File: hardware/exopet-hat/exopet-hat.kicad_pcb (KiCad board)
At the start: 2 copper layers, 65 x 56 mm, 71 parts, among them J1 BarrelJack_CUI_PJ-102AH_Horiz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, J10 TerminalBlock_Phoenix_PT-1,5-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, J11 TerminalBlock_Phoenix_PT-1,5-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, J13 TerminalBlock_Phoenix_PT-1,5-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, J14 TerminalBlock_Phoenix_PT-1,5-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, J3 PinSocket_2x20_P2.54mm_Vertic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, J4 TerminalBlock_Phoenix_PT-1,5-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, J8 TerminalBlock_Phoenix_PT-1,5-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, J9 TerminalBlock_Phoenix_PT-1,5-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, K1 Relay_SPDT_Omron-G5LE-1, K2 Relay_SPDT_Omron-G5LE-1, K3 Relay_SPDT_Omron-G5LE-1, K4 Relay_SPDT_Omron-G5LE-1, Q1 TO-252-2, U2 SOIC-16_3.9x9.9mm_P1.27mm, U4 SOIC-8_3.9x4.9mm_P1.27mm, U5 D_SOD-323, U6 SOT-23-6

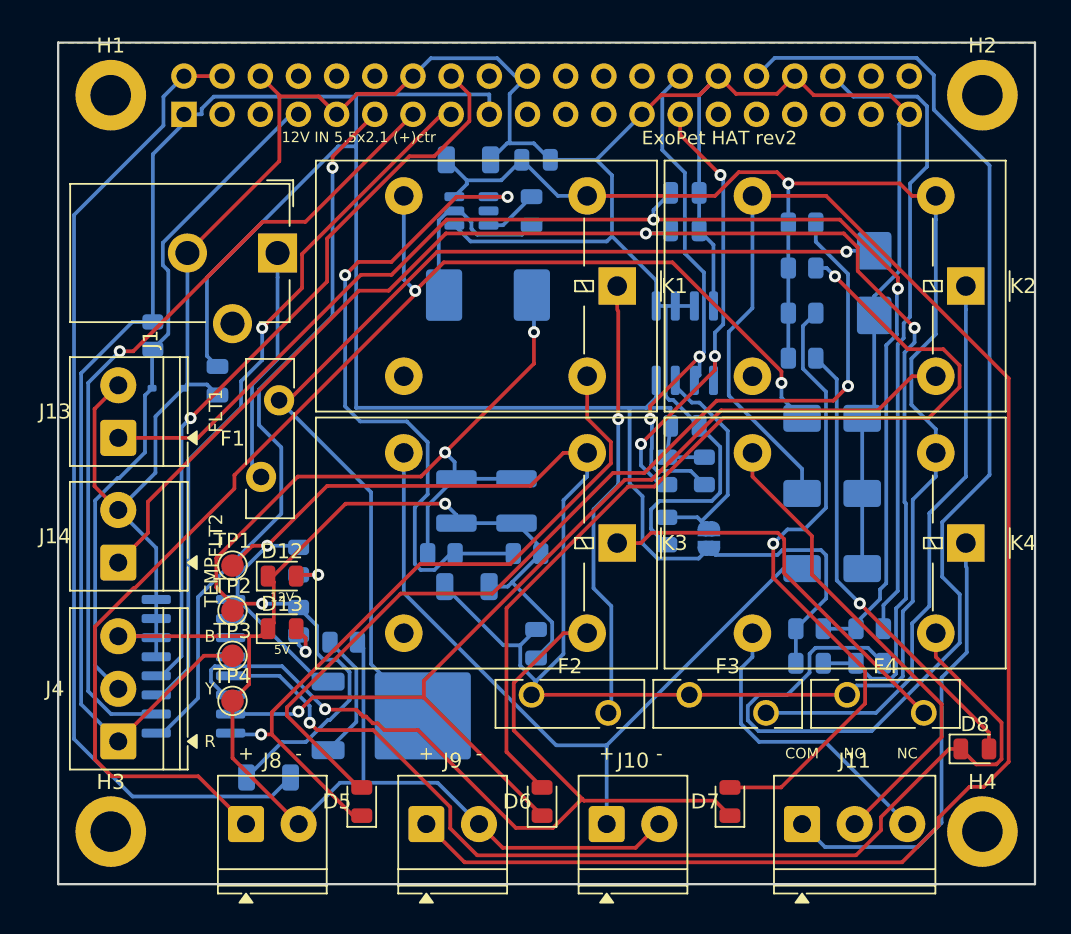
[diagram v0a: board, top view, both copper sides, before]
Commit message: HAT rev 2: apply all 7 fresh-eyes review fixes
- D3 B550C safety diode replaces R21 (HAT-guide compliant back-power;
  kills the USB-C->barrel-jack back-feed; no 2A jumper in the 5V path);
  buck setpoint raised to 5.40V pre-diode (R17 13.3k->12.4k)
- C17 75pF feedforward across R16 (TI Table 7-2, all-ceramic Cout)
- C1 100uF 25V low-profile SMD electrolytic restores input bulk
- F1 MF-RG500 -> MF-RG700 (hold current derating vs ~4.6A full load)
- D1 TVS moved from 40mm away to the input corner it protects
- ORDERING.md/BRINGUP.md rewritten for the new power architecture
- float conditioning resistors relocated near their terminals

New gate: check_drc_sanity.py re-measures every claimed clearance pair
from board geometry — kicad-cli emits phantom violations citing items
20.6mm apart as 0.055mm; phantoms are excused only with printed
measured proof. Preflight fully green: 69 parts, 212-pin golden audit,
DRC 0 real / 0 unconnected.

Co-Authored-By: Claude Fable 5 <noreply@anthropic.com>
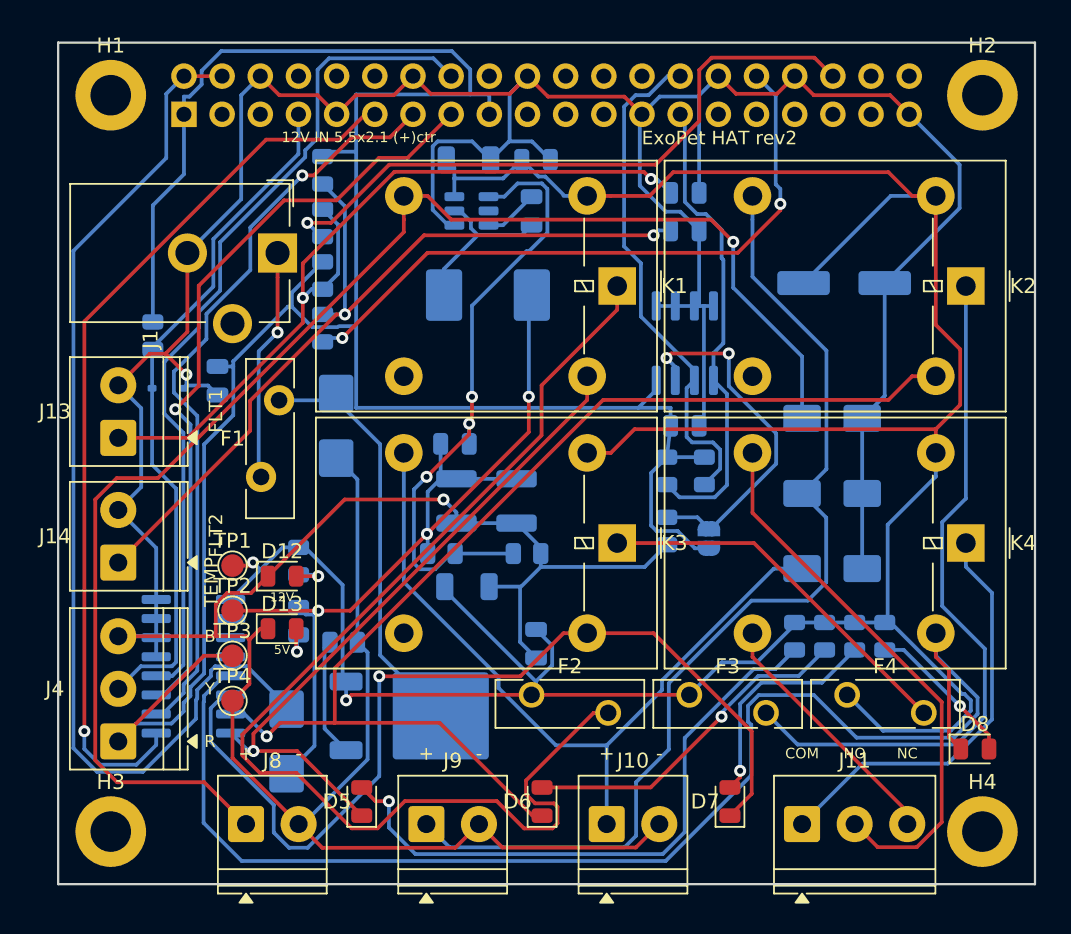
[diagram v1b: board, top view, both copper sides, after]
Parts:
- removed R21: R_1206_3216Metric, Resistor_SMD:R_1206_3216Metric
- added C1: CP_Elec_6.3x7.7, Capacitor_SMD:CP_Elec_6.3x7.7, B.Cu at (52.3, 16.0)
- added C17: C_0805_2012Metric, Capacitor_SMD:C_0805_2012Metric, B.Cu at (26.4, 26.7)
- added D3: D_SMB, Diode_SMD:D_SMB, B.Cu at (15.2, 46.5)
- moved R11 46.1 mm to (17.6, 8.50), turned to -90 degrees
- moved R12 45.3 mm to (17.6, 12.0), turned to -90 degrees
- moved R13 42.7 mm to (17.6, 19.0), turned to -90 degrees
- moved R10 40.0 mm to (17.6, 15.5), turned to -90 degrees
- moved D1 37.0 mm to (18.5, 25.5)
- moved R5 27.5 mm to (49.0, 39.5), turned to -90 degrees
- moved R6 24.5 mm to (51.0, 39.5), turned to -90 degrees
- moved R7 21.8 mm to (53.0, 39.5), turned to -90 degrees
- moved R8 19.3 mm to (55.0, 39.5), turned to -90 degrees
- moved Q1 1.20 mm to (24.2, 44.8)
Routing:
- net CH1_FUSED: track 29.6 -> 78.0 mm, vias 1 -> 0
- net CH2_OUT: track 113.0 -> 68.3 mm
- net +12V_F: track 68.6 -> 28.1 mm, vias 1 -> 0
- net LED2_A: track 62.8 -> 22.7 mm
- net FLOAT2_GPIO: track 83.5 -> 43.7 mm, vias 0 -> 2
- net FLOAT2_SW: track 97.5 -> 57.8 mm
- net FLOAT1_SW: track 88.3 -> 54.7 mm
- net LED3_A: track 42.9 -> 15.0 mm
- net LED1_A: track 65.4 -> 41.0 mm
- net LED4_A: track 30.8 -> 10.2 mm
- net RLY4_DRV: track 71.9 -> 87.6 mm, vias 1 -> 0
- net +12V: track 179.1 -> 194.0 mm
- net +3V3: track 179.2 -> 165.6 mm
- net GPIO17: track 48.7 -> 60.0 mm
- net EEPROM_WP: track 15.0 -> 24.0 mm, vias 0 -> 2
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
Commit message: HAT rev 2: round-2 review fixes — buck corners + F1 BOM pin
10uH inductor (HS current-limit margin at tolerance corners), 25V X7R
output caps (DC-bias derating), 12.7k FB (5.29V — Pi stays under +5%
at light load), F1 BOM unpinned (was still the 5A part code after the
7A value change — panel caught the incomplete fix). GPIO23 gets a
locked pre-route (down the J3 column midline, via, U2 escape) after
repeated seed strandings; float debounce caps C5/C6 move beside their
terminals. DRC sanity filter generalized to all geometric violation
types (phantoms now include shorting/mask reports citing items 3-20mm
apart). Preflight fully green; review package rebuilt with round-2
findings + honest lens coverage map for the human reviewer.

Co-Authored-By: Claude Fable 5 <noreply@anthropic.com>
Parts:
- moved C6 39.8 mm to (7.60, 33.0)
- moved C5 38.9 mm to (7.60, 28.7)
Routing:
- net CH1_FUSED: track 78.0 -> 37.1 mm
- net FLOAT1_SW: track 54.7 -> 27.4 mm, vias 2 -> 0
- net +12V: track 194.0 -> 173.9 mm
- net RLY2_DRV: track 75.9 -> 91.7 mm
- net RLY4_DRV: track 87.6 -> 74.6 mm, vias 0 -> 1
- net +5V: track 70.7 -> 58.5 mm, vias 0 -> 1
- net EEPROM_SDA: track 31.5 -> 42.8 mm
- net FLOAT1_GPIO: track 43.3 -> 54.3 mm, vias 1 -> 3
- net CH1_OUT: track 96.3 -> 105.8 mm
- net CH2_FUSED: track 46.7 -> 55.4 mm
- net LED1_A: track 41.0 -> 32.6 mm
- net CH2_OUT: track 68.3 -> 60.2 mm
- net BUCK_FB: track 41.7 -> 33.6 mm, vias 3 -> 2
- net +5V_BUCK: track 59.5 -> 66.5 mm
- net GND: track 318.2 -> 324.6 mm, vias 2 -> 0
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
